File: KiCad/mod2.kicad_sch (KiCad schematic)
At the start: 49 parts, among them M3 Fan_4pin, M4 Fan_4pin, U2 ZD25Q64BSIGT

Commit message: Add most passive component footprints
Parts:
- C34, C35, C36, C37, C38, C39, C40, C41, C42, C43, C44, C45, C46, C47, C48, C49, C50, C51, C52, C53, C54, C55, C56: footprint Capacitor_SMD:C_0603_1608Metric -> Capacitor_SMD:C_0402_1005Metric
- D5, D6: footprint (none) -> LED_SMD:LED_0603_1608Metric
- D7, D8: footprint (none) -> Diode_SMD:D_SOD-123
- M3, M4: footprint (none) -> Connector:FanPinHeader_1x04_P2.54mm_Vertical
- R27, R39: value 510R -> 2.2k; footprint (none) -> Resistor_SMD:R_0402_1005Metric
- R28, R29, R30, R32, R33, R34, R35, R36, R38, R40, R43, R44: footprint (none) -> Resistor_SMD:R_0402_1005Metric
- R31: footprint (none) -> Resistor_SMD:R_0805_2012Metric
- R37, R41, R42: value 21.5k -> 22k; footprint (none) -> Resistor_SMD:R_0402_1005Metric
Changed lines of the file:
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@@
 			)
 		)
-		(property "Footprint" "Capacitor_SMD:C_0603_1608Metric"
+		(property "Footprint" "Capacitor_SMD:C_0402_1005Metric"
 			(at 237.49 181.61 0)
 			(effects
@@
 			)
 		)
-		(property "Footprint" "Capacitor_SMD:C_0603_1608Metric"
+		(property "Footprint" "Capacitor_SMD:C_0402_1005Metric"
 			(at 237.49 163.83 0)
 			(effects
@@
 			)
 		)
-		(property "Footprint" "Capacitor_SMD:C_0603_1608Metric"
+		(property "Footprint" "Capacitor_SMD:C_0402_1005Metric"
 			(at 237.49 196.85 0)
 			(effects
@@
 		(dnp no)
 		(property "Reference" "C46"
-			(at 235.458 175.514 90)
+			(at 234.188 175.514 90)
 			(effects
 				(font
@@
 			)
 		)
-		(property "Footprint" "Capacitor_SMD:C_0603_1608Metric"
+		(property "Footprint" "Capacitor_SMD:C_0402_1005Metric"
 			(at 237.49 176.53 0)
 			(effects
@@
 			)
 		)
-		(property "Footprint" ""
+		(property "Footprint" "Resistor_SMD:R_0402_1005Metric"
 			(at 337.82 67.31 0)
 			(effects
@@
 			)
 		)
-		(property "Footprint" "Capacitor_SMD:C_0603_1608Metric"
+		(property "Footprint" "Capacitor_SMD:C_0402_1005Metric"
 			(at 353.06 259.08 0)
 			(effects
@@
 			)
 		)
-		(property "Footprint" ""
+		(property "Footprint" "Resistor_SMD:R_0402_1005Metric"
 			(at 330.2 289.56 0)
 			(effects
@@
 			)
 		)
-		(property "Footprint" "Capacitor_SMD:C_0603_1608Metric"
+		(property "Footprint" "Capacitor_SMD:C_0402_1005Metric"
 			(at 237.49 120.65 0)
 			(effects
@@
 			)
 		)
-		(property "Footprint" ""
+		(property "Footprint" "LED_SMD:LED_0603_1608Metric"
 			(at 223.52 90.17 0)
 			(effects
@@
 			)
 		)
-		(property "Value" "510R"
+		(property "Value" "2.2k"
 			(at 342.9 161.29 90)
 			(effects
@@
 			)
 		)
-		(property "Footprint" ""
+		(property "Footprint" "Resistor_SMD:R_0402_1005Metric"
 			(at 342.9 163.83 0)
 			(effects
@@
 			)
 		)
-		(property "Footprint" "Capacitor_SMD:C_0603_1608Metric"
+		(property "Footprint" "Capacitor_SMD:C_0402_1005Metric"
 			(at 237.49 194.31 0)
 			(effects
@@
 			)
 		)
-		(property "Footprint" "Capacitor_SMD:C_0603_1608Metric"
+		(property "Footprint" "Capacitor_SMD:C_0402_1005Metric"
 			(at 237.49 128.27 0)
 			(effects
@@
 			)
 		)
-		(property "Footprint" ""
+		(property "Footprint" "Resistor_SMD:R_0402_1005Metric"
 			(at 334.01 138.43 0)
 			(effects
@@
 			)
 		)
-		(property "Footprint" "Capacitor_SMD:C_0603_1608Metric"
+		(property "Footprint" "Capacitor_SMD:C_0402_1005Metric"
 			(at 237.49 189.23 0)
 			(effects
@@
 		(dnp no)
 		(property "Reference" "C47"
-			(at 235.458 178.054 90)
+			(at 234.188 178.054 90)
 			(effects
 				(font
@@
 			)
 		)
-		(property "Footprint" "Capacitor_SMD:C_0603_1608Metric"
+		(property "Footprint" "Capacitor_SMD:C_0402_1005Metric"
 			(at 237.49 179.07 0)
 			(effects
@@
 		(dnp no)
 		(property "Reference" "C45"
-			(at 235.458 172.974 90)
+			(at 234.188 172.974 90)
 			(effects
 				(font
@@
 			)
 		)
-		(property "Footprint" "Capacitor_SMD:C_0603_1608Metric"
+		(property "Footprint" "Capacitor_SMD:C_0402_1005Metric"
 			(at 237.49 173.99 0)
 			(effects
@@
 			)
 		)
-		(property "Footprint" "Capacitor_SMD:C_0603_1608Metric"
+		(property "Footprint" "Capacitor_SMD:C_0402_1005Metric"
 			(at 384.81 57.15 0)
 			(effects
@@
 			)
 		)
-		(property "Footprint" ""
+		(property "Footprint" "Diode_SMD:D_SOD-123"
 			(at 341.63 57.15 0)
 			(effects
@@
 			)
 		)
-		(property "Footprint" "Capacitor_SMD:C_0603_1608Metric"
+		(property "Footprint" "Capacitor_SMD:C_0402_1005Metric"
 			(at 237.49 107.95 0)
 			(effects
@@
 			)
 		)
-		(property "Footprint" ""
+		(property "Footprint" "Connector:FanPinHeader_1x04_P2.54mm_Vertical"
 			(at 417.83 64.516 0)
 			(effects
@@
 			)
 		)
-		(property "Value" "21.5k"
+		(property "Value" "22k"
 			(at 339.852 64.262 90)
 			(effects
@@
 			)
 		)
-		(property "Footprint" ""
+		(property "Footprint" "Resistor_SMD:R_0402_1005Metric"
 			(at 337.82 62.23 0)
 			(effects
@@
 		(dnp no)
 		(property "Reference" "C44"
-			(at 235.458 170.434 90)
+			(at 234.188 170.434 90)
 			(effects
 				(font
@@
 			)
 		)
-		(property "Footprint" "Capacitor_SMD:C_0603_1608Metric"
+		(property "Footprint" "Capacitor_SMD:C_0402_1005Metric"
 			(at 237.49 171.45 0)
 			(effects
@@
 			)
 		)
-		(property "Footprint" "Capacitor_SMD:C_0603_1608Metric"
+		(property "Footprint" "Capacitor_SMD:C_0402_1005Metric"
 			(at 237.49 130.81 0)
 			(effects
@@
 			)
 		)
-		(property "Footprint" ""
+		(property "Footprint" "Resistor_SMD:R_0402_1005Metric"
 			(at 237.49 275.59 0)
 			(effects
@@
 			)
 		)
-		(property "Footprint" ""
+		(property "Footprint" "Resistor_SMD:R_0402_1005Metric"
 			(at 335.28 262.89 0)
 			(effects
@@
 			)
 		)
-		(property "Footprint" ""
+		(property "Footprint" "Connector:FanPinHeader_1x04_P2.54mm_Vertical"
 			(at 363.22 64.516 0)
 			(effects
@@
 			)
 		)
-		(property "Footprint" ""
+		(property "Footprint" "Diode_SMD:D_SOD-123"
 			(at 396.24 57.15 0)
 			(effects
@@
 			)
 		)
-		(property "Footprint" ""
+		(property "Footprint" "Resistor_SMD:R_0805_2012Metric"
 			(at 289.56 78.74 0)
 			(effects
@@
 			)
 		)
-		(property "Footprint" "Capacitor_SMD:C_0603_1608Metric"
+		(property "Footprint" "Capacitor_SMD:C_0402_1005Metric"
 			(at 237.49 161.29 0)
 			(effects
@@
 			)
 		)
-		(property "Footprint" ""
+		(property "Footprint" "Resistor_SMD:R_0402_1005Metric"
 			(at 237.49 237.49 0)
 			(effects
@@
 			)
 		)
-		(property "Footprint" ""
+		(property "Footprint" "Resistor_SMD:R_0402_1005Metric"
 			(at 330.2 262.89 0)
 			(effects
@@
 			)
 		)
-		(property "Footprint" ""
+		(property "Footprint" "Resistor_SMD:R_0402_1005Metric"
 			(at 334.01 140.97 0)
 			(effects
@@
 			)
 		)
-		(property "Footprint" ""
+		(property "Footprint" "Resistor_SMD:R_0402_1005Metric"
 			(at 237.49 313.69 0)
 			(effects
@@
 			)
 		)
-		(property "Footprint" "Capacitor_SMD:C_0603_1608Metric"
+		(property "Footprint" "Capacitor_SMD:C_0402_1005Metric"
 			(at 237.49 184.15 0)
 			(effects
@@
 			)
 		)
-		(property "Footprint" "Capacitor_SMD:C_0603_1608Metric"
+		(property "Footprint" "Capacitor_SMD:C_0402_1005Metric"
 			(at 334.01 57.15 0)
 			(effects
@@
 			)
 		)
-		(property "Footprint" ""
+		(property "Footprint" "Resistor_SMD:R_0402_1005Metric"
 			(at 406.4 57.15 0)
 			(effects
@@
 			)
 		)
-		(property "Footprint" ""
+		(property "Footprint" "Resistor_SMD:R_0402_1005Metric"
 			(at 392.43 67.31 0)
 			(effects
@@
 			)
 		)
-		(property "Footprint" "Capacitor_SMD:C_0603_1608Metric"
+		(property "Footprint" "Capacitor_SMD:C_0402_1005Metric"
 			(at 237.49 151.13 0)
 			(effects
@@
 			)
 		)
-		(property "Value" "21.5k"
+		(property "Value" "22k"
 			(at 391.16 73.6599 0)
 			(effects
@@
 			)
 		)
-		(property "Footprint" ""
+		(property "Footprint" "Resistor_SMD:R_0402_1005Metric"
 			(at 388.62 72.39 0)
 			(effects
@@
 			)
 		)
-		(property "Value" "21.5k"
+		(property "Value" "22k"
 			(at 394.462 64.262 90)
 			(effects
@@
 			)
 		)
-		(property "Footprint" ""
+		(property "Footprint" "Resistor_SMD:R_0402_1005Metric"
 			(at 392.43 62.23 0)
 			(effects
@@
 			)
 		)
-		(property "Footprint" "Capacitor_SMD:C_0603_1608Metric"
+		(property "Footprint" "Capacitor_SMD:C_0402_1005Metric"
 			(at 237.49 153.67 0)
 			(effects
@@
 			)
 		)
-		(property "Value" "510R"
+		(property "Value" "2.2k"
 			(at 226.06 83.8199 0)
 			(effects
@@
 			)
 		)
-		(property "Footprint" ""
+		(property "Footprint" "Resistor_SMD:R_0402_1005Metric"
 			(at 223.52 82.55 0)
 			(effects
@@
 			)
 		)
-		(property "Footprint" "Capacitor_SMD:C_0603_1608Metric"
+		(property "Footprint" "Capacitor_SMD:C_0402_1005Metric"
 			(at 237.49 186.69 0)
 			(effects
@@
 			)
 		)
-		(property "Footprint" "Capacitor_SMD:C_0603_1608Metric"
+		(property "Footprint" "Capacitor_SMD:C_0402_1005Metric"
 			(at 237.49 118.11 0)
 			(effects
@@
 			)
 		)
-		(property "Footprint" ""
+		(property "Footprint" "LED_SMD:LED_0603_1608Metric"
 			(at 334.01 163.83 0)
 			(effects
@@
 			)
 		)
-		(property "Footprint" "Capacitor_SMD:C_0603_1608Metric"
+		(property "Footprint" "Capacitor_SMD:C_0402_1005Metric"
 			(at 237.49 110.49 0)
 			(effects
@@
 			)
 		)
-		(property "Footprint" ""
+		(property "Footprint" "Resistor_SMD:R_0402_1005Metric"
 			(at 351.79 57.15 0)
 			(effects

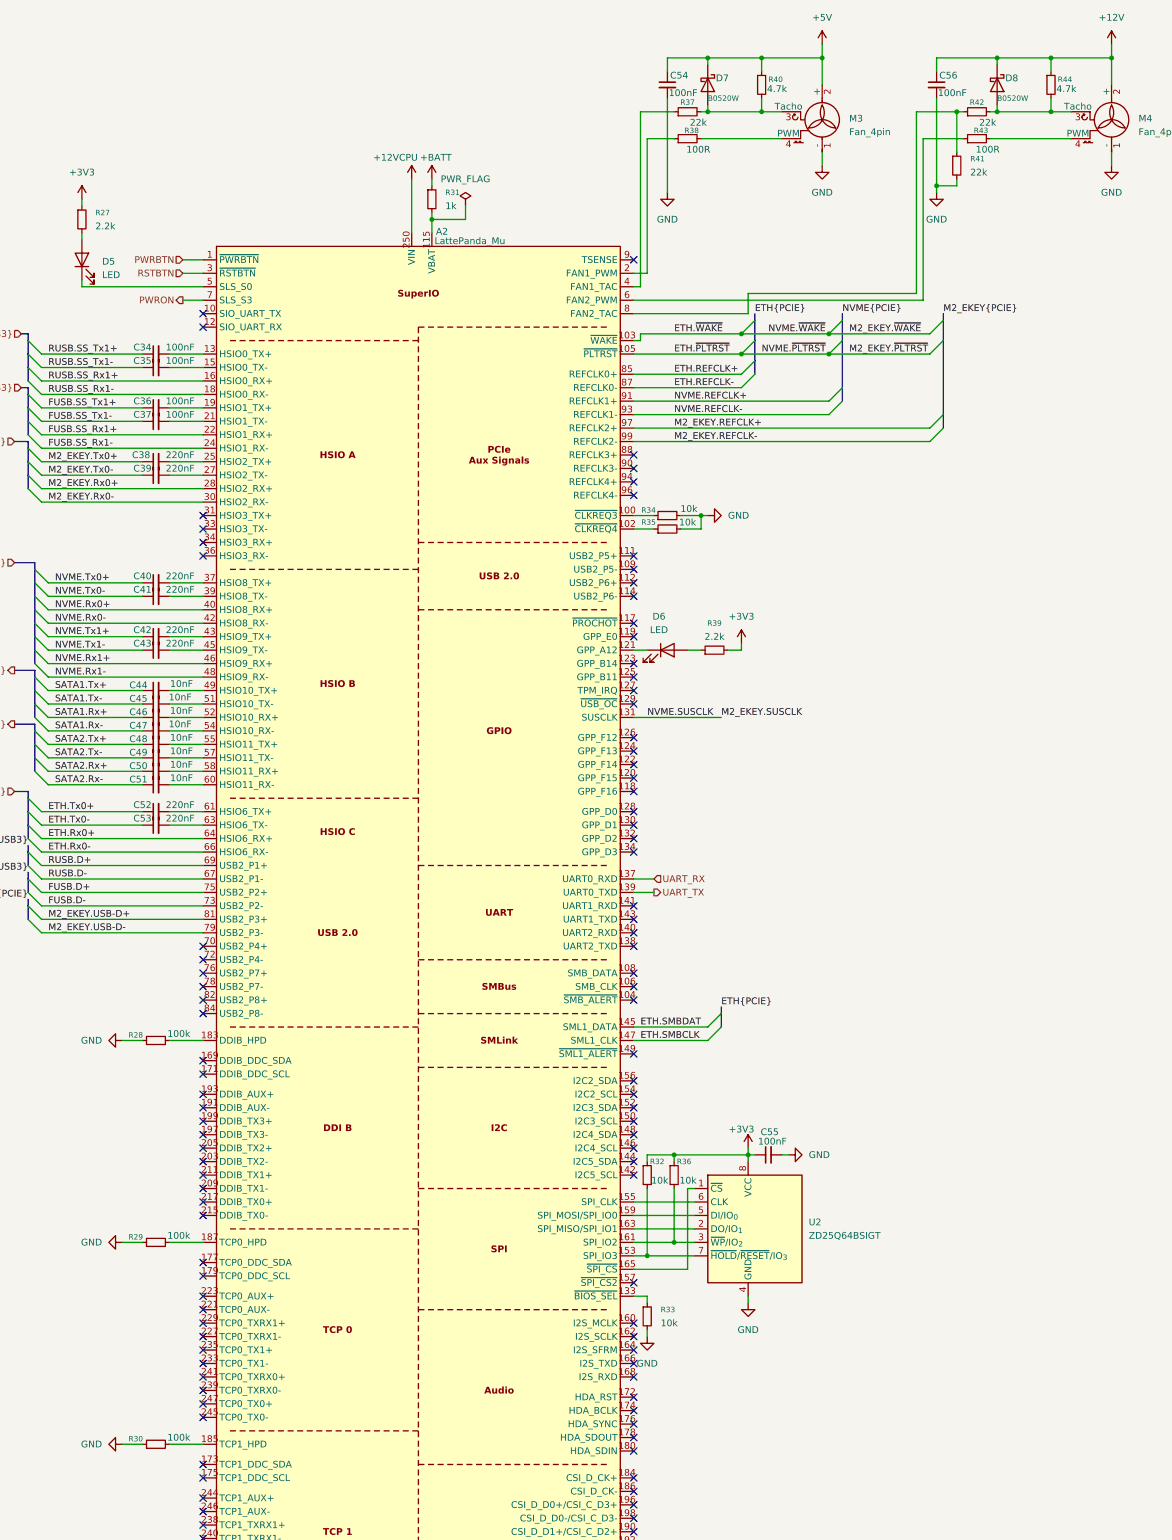
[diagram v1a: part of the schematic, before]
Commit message: Finish fixing footprints
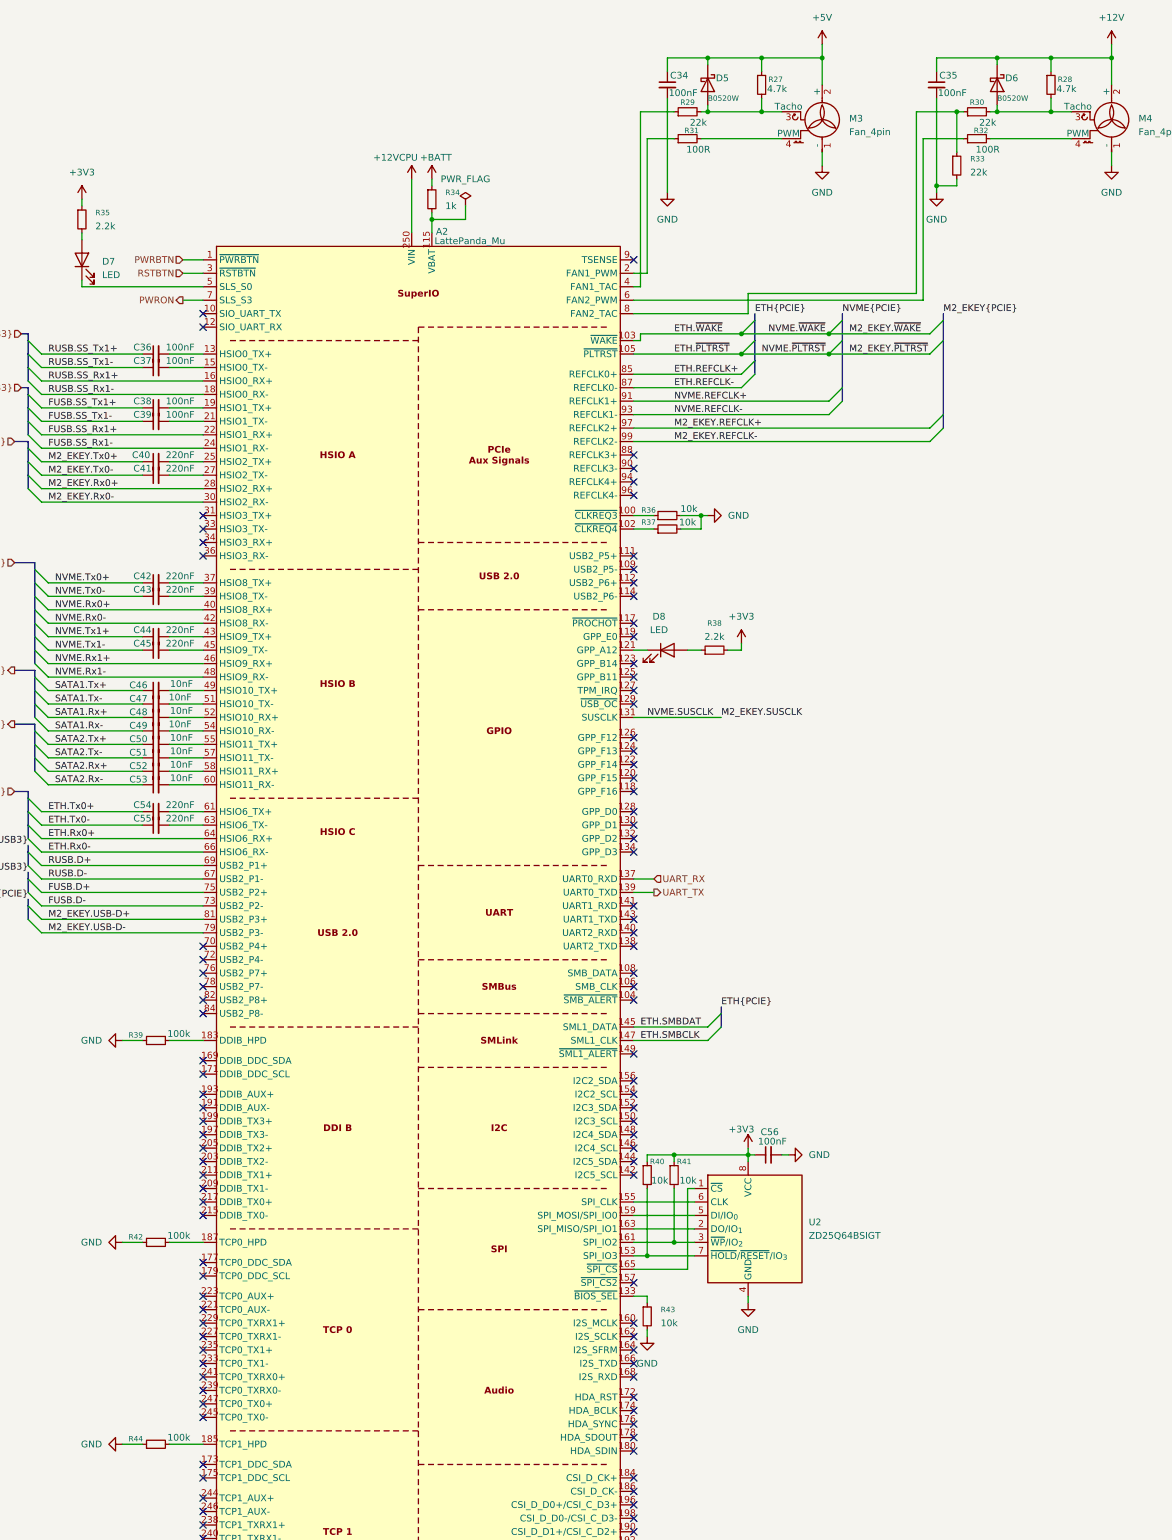
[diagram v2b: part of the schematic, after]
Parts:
- renumbered C54 to C34, C56 to C35, C34 to C36, C35 to C37, C36 to C38, C37 to C39, C38 to C40, C39 to C41, C40 to C42, C41 to C43, C42 to C44, C43 to C45, C44 to C46, C45 to C47, C46 to C48, C47 to C49, C48 to C50, C49 to C51, C50 to C52, C51 to C53, C52 to C54, C53 to C55, C55 to C56, D7 to D5, D8 to D6, D5 to D7, D6 to D8, R40 to R27, R44 to R28, R37 to R29, R42 to R30, R38 to R31, R43 to R32, R41 to R33, R31 to R34, R27 to R35, R34 to R36, R35 to R37, R39 to R38, R28 to R39, R32 to R40, R36 to R41, R29 to R42, R33 to R43, R30 to R44

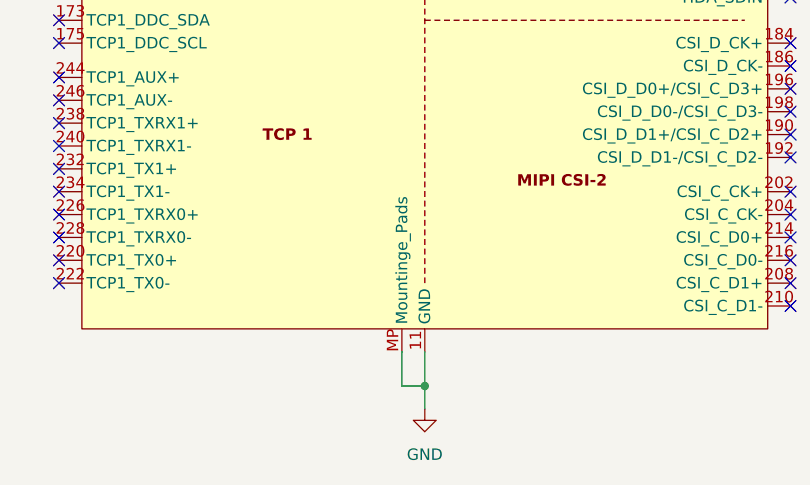
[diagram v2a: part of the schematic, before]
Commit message: Fix more footprint issues, continue laying out components
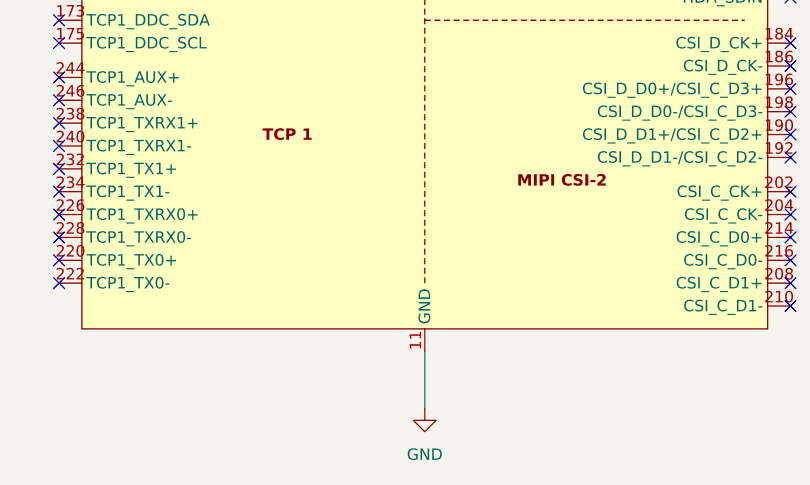
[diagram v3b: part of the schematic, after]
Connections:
- net GND: no longer A2.MP (Mountinge_Pads)
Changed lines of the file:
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@@
 	)
 	(junction
-		(at 287.02 358.14)
-		(diameter 0)
-		(color 0 0 0 0)
-	)
-	(junction
 		(at 364.49 107.95)
 		(diameter 0)
@@
 	(wire
 		(pts
-			(xy 287.02 354.33) (xy 287.02 358.14)
+			(xy 287.02 354.33) (xy 287.02 360.68)
 		)
 		(stroke
@@
 	(wire
 		(pts
-			(xy 287.02 358.14) (xy 287.02 360.68)
-		)
-		(stroke
-			(width 0)
-			(type default)
-		)
-	)
-	(wire
-		(pts
 			(xy 295.91 82.55) (xy 289.56 82.55)
 		)
@@
 	(wire
 		(pts
-			(xy 284.48 358.14) (xy 287.02 358.14)
-		)
-		(stroke
-			(width 0)
-			(type default)
-		)
-	)
-	(wire
-		(pts
 			(xy 215.9 107.95) (xy 234.95 107.95)
 		)
@@
 		)
 	)
-	(wire
-		(pts
-			(xy 284.48 354.33) (xy 284.48 358.14)
-		)
-		(stroke
-			(width 0)
-			(type default)
-		)
-	)
 	(bus
 		(pts
@@
 		(pin "248"
 		)
-		(pin "MP"
-		)
 		(pin "154"

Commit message: Place STM32 and fix cpu fan headers
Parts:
- M3: footprint Connector:FanPinHeader_1x04_P2.54mm_Vertical -> Connector_JST:JST_PH_B4B-PH-K_1x04_P2.00mm_Vertical
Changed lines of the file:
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@@
 			)
 		)
-		(property "Footprint" "Connector:FanPinHeader_1x04_P2.54mm_Vertical"
+		(property "Footprint" "Connector_JST:JST_PH_B4B-PH-K_1x04_P2.00mm_Vertical"
 			(at 363.22 64.516 0)
 			(effects

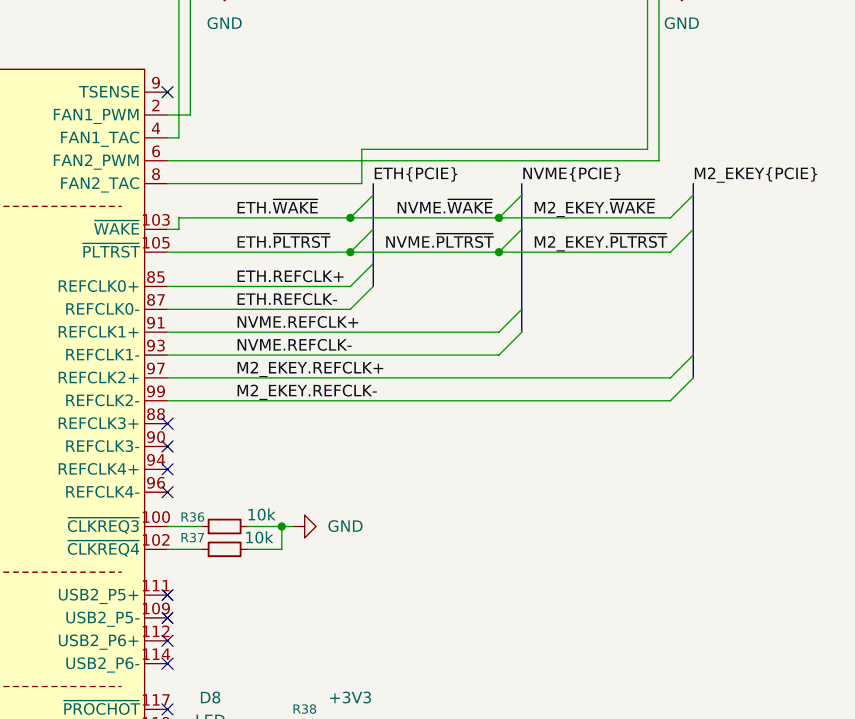
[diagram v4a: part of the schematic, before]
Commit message: Finish connecting x1 slot. Add pcie clkreq lines
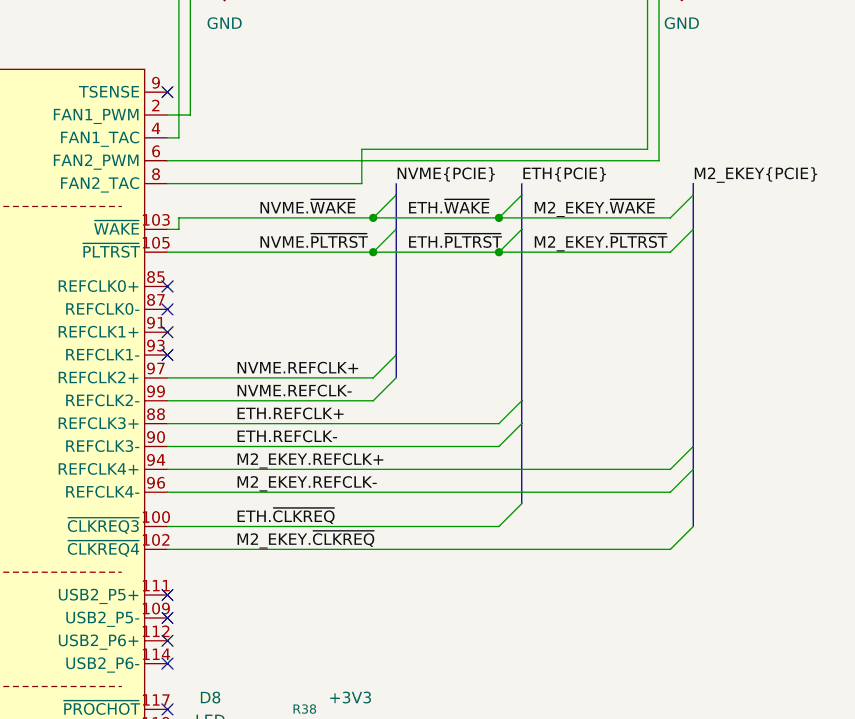
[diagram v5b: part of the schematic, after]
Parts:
- removed R36, R37: 10k, Resistor_SMD:R_0402_1005Metric, symbol Device:R_Small
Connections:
- net ETH.REFCLK+: now also A2.88 (REFCLK3+); no longer A2.85 (REFCLK0+)
- net ETH.REFCLK-: now also A2.90 (REFCLK3-); no longer A2.87 (REFCLK0-)
- net M2_EKEY.REFCLK+: now also A2.94 (REFCLK4+); no longer A2.97 (REFCLK2+)
- net M2_EKEY.REFCLK-: now also A2.96 (REFCLK4-); no longer A2.99 (REFCLK2-)
- net NVME.REFCLK+: now also A2.97 (REFCLK2+); no longer A2.91 (REFCLK1+)
- net NVME.REFCLK-: now also A2.99 (REFCLK2-); no longer A2.93 (REFCLK1-)
- net ETH.~{CLKREQ}: now reaches A2.100 (~{CLKREQ3})
- net M2_EKEY.~{CLKREQ}: now reaches A2.102 (~{CLKREQ4})
